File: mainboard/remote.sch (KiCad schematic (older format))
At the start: 14 parts, among them J1 Conn_01x03, J2 Conn_01x02, J4 Conn_01x03, J5 Conn_01x03, J6 Conn_01x02, J7 Conn_01x03, U7 COM-09032, U8 COM-09032

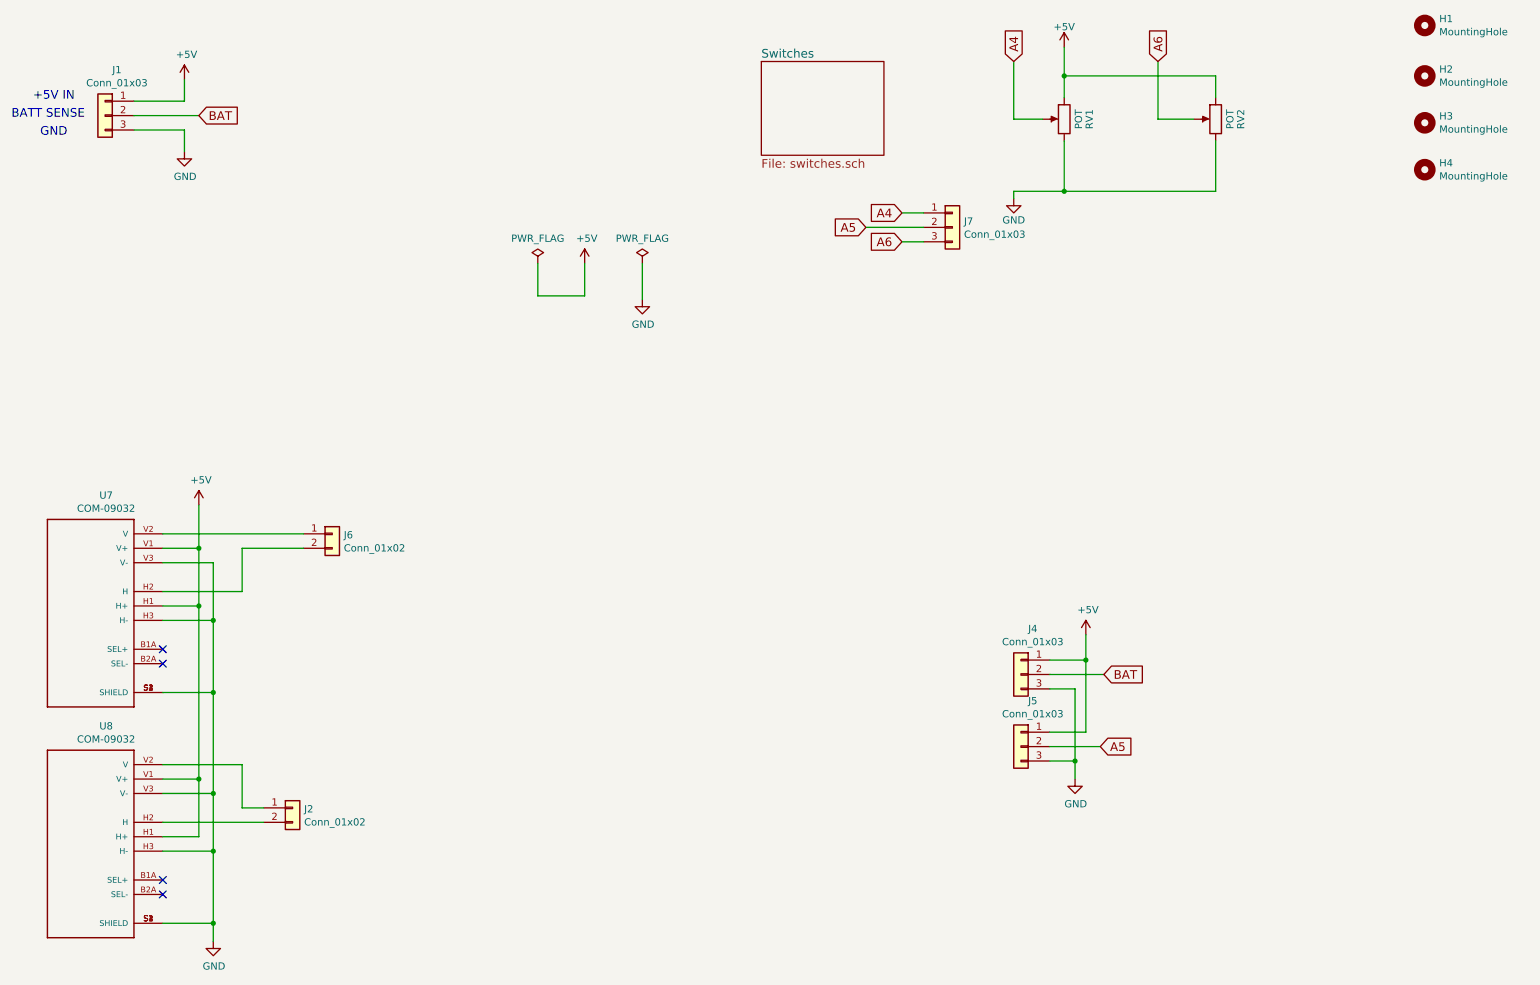
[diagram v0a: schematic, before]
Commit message: Update for I2C display.
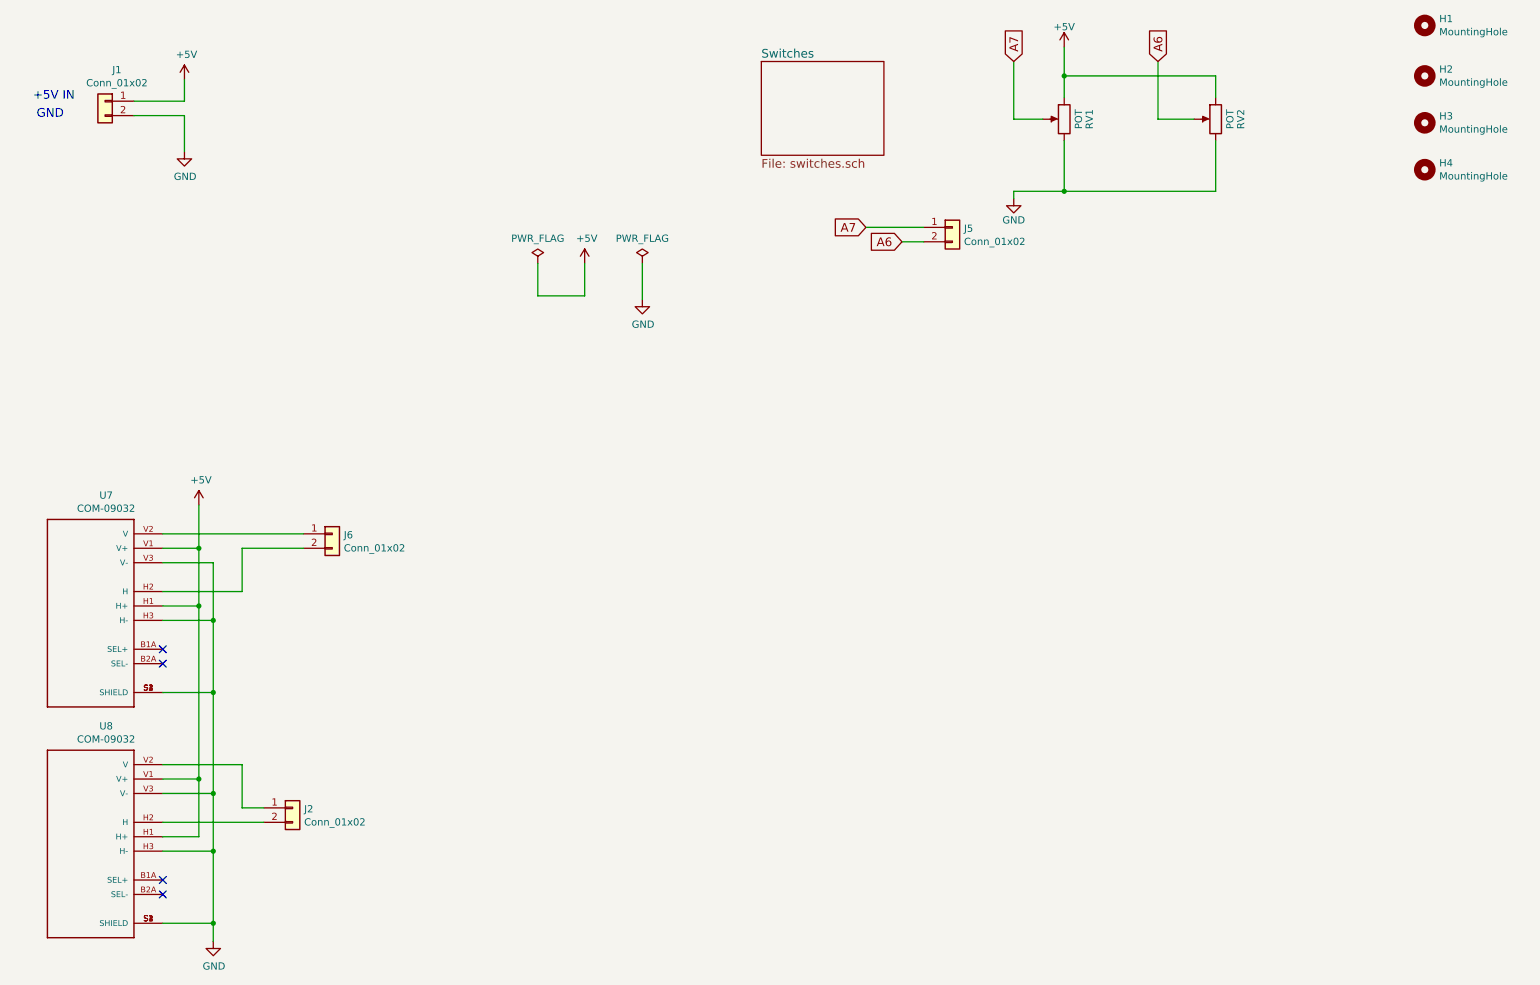
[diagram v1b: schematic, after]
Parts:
- removed J1, J4, J5, J7: Conn_01x03, Milling:JST_XH_B03B-XH-A_1x03_P2.50mm_Vertical_Milling, symbol Connector_Generic:Conn_01x03
- added J1, J5: Conn_01x02, Milling:JST_XH_B02B-XH-A_1x02_P2.50mm_Vertical_Milling, symbol Connector_Generic:Conn_01x02
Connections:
- net +5V: now also J1.1 (Pin_1)
- net A6: now also J5.2 (Pin_2)
- net GND: now also J1.2 (Pin_2)
- net A4 renamed A7
- net A7: now also J5.1 (Pin_1)
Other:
- note removed: "BATT SENSE"
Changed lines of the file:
@@
 	8700 1375 8450 1375
 Text GLabel 7450 975  1    60   Input ~ 0
-A4
+A7
 Text GLabel 8450 975  1    60   Input ~ 0
 A6
@@
 A6
 Text GLabel 6425 2125 0    60   Input ~ 0
-A5
-Text GLabel 6675 2025 0    60   Input ~ 0
-A4
+A7
 Wire Wire Line
 	7450 1875 7450 1925
@@
 	7800 1875 8850 1875
 $Comp
-L Connector_Generic:Conn_01x03 J1
-U 1 1 5E3721E4
-P 1150 1350
-F 0 "J1" H 1068 1667 50  0000 C CNN
-F 1 "Conn_01x03" H 1068 1576 50  0000 C CNN
-F 2 "Milling:JST_XH_B03B-XH-A_1x03_P2.50mm_Vertical_Milling" H 1150 1350 50  0001 C CNN
-F 3 "~" H 1150 1350 50  0001 C CNN
-	1    1150 1350
-	-1   0    0    -1
-$EndComp
-$Comp
 L power:+5V #PWR0109
 U 1 1 5E3728A7
@@
 	1    0    0    -1
 $EndComp
-Wire Wire Line
-	1700 1600 1700 1450
-Wire Wire Line
-	1700 1450 1350 1450
-Text GLabel 8050 5725 2    60   Input ~ 0
-A5
-Wire Wire Line
-	1800 1350 1350 1350
 Text Notes 650  1250 0    60   ~ 0
 +5V IN
-Text Notes 700  1500 0    60   ~ 0
+Text Notes 675  1375 0    60   ~ 0
 GND
-Text Notes 500  1375 0    60   ~ 0
-BATT SENSE
 $Comp
 L power:PWR_FLAG #FLG0101
@@
 	6825 2125 6425 2125
 Wire Wire Line
-	6675 2025 6825 2025
-Wire Wire Line
 	1550 4650 2100 4650
-$Comp
-L Connector_Generic:Conn_01x03 J4
-U 1 1 5E698090
-P 7500 5225
-F 0 "J4" H 7418 5542 50  0000 C CNN
-F 1 "Conn_01x03" H 7418 5451 50  0000 C CNN
-F 2 "Milling:JST_XH_B03B-XH-A_1x03_P2.50mm_Vertical_Milling" H 7500 5225 50  0001 C CNN
-F 3 "~" H 7500 5225 50  0001 C CNN
-	1    7500 5225
-	-1   0    0    -1
-$EndComp
-$Comp
-L Connector_Generic:Conn_01x03 J5
-U 1 1 5E698C2B
-P 7500 5725
-F 0 "J5" H 7418 6042 50  0000 C CNN
-F 1 "Conn_01x03" H 7418 5951 50  0000 C CNN
-F 2 "Milling:JST_XH_B03B-XH-A_1x03_P2.50mm_Vertical_Milling" H 7500 5725 50  0001 C CNN
-F 3 "~" H 7500 5725 50  0001 C CNN
-	1    7500 5725
-	-1   0    0    -1
-$EndComp
-$Comp
-L power:+5V #PWR0130
-U 1 1 5E6B17BB
-P 7950 4950
-F 0 "#PWR0130" H 7950 4800 50  0001 C CNN
-F 1 "+5V" H 7965 5123 50  0000 C CNN
-F 2 "" H 7950 4950 50  0001 C CNN
-F 3 "" H 7950 4950 50  0001 C CNN
-	1    7950 4950
-	1    0    0    -1
-$EndComp
-Wire Wire Line
-	7950 4950 7950 5125
-Wire Wire Line
-	7950 5625 7700 5625
-Wire Wire Line
-	7700 5125 7950 5125
-Connection ~ 7950 5125
-Wire Wire Line
-	7950 5125 7950 5625
-$Comp
-L power:GND #PWR0131
-U 1 1 5E6BD4D9
-P 7875 5950
-F 0 "#PWR0131" H 7875 5700 50  0001 C CNN
-F 1 "GND" H 7880 5777 50  0000 C CNN
-F 2 "" H 7875 5950 50  0001 C CNN
-F 3 "" H 7875 5950 50  0001 C CNN
-	1    7875 5950
-	1    0    0    -1
-$EndComp
-Wire Wire Line
-	7875 5950 7875 5825
-Wire Wire Line
-	7875 5325 7700 5325
-Wire Wire Line
-	7700 5825 7875 5825
-Connection ~ 7875 5825
-Wire Wire Line
-	7875 5825 7875 5325
-Wire Wire Line
-	8050 5725 7700 5725
-Text GLabel 8075 5225 2    60   Input ~ 0
-BAT
-Wire Wire Line
-	8075 5225 7700 5225
-Text GLabel 1800 1350 2    60   Input ~ 0
-BAT
 $Comp
 L Connector_Generic:Conn_01x02 J6
@@
 	2100 6150 2250 6150
 $Comp
-L Connector_Generic:Conn_01x03 J7
-U 1 1 5E7123B6
+L Connector_Generic:Conn_01x02 J1
+U 1 1 5E3EC8B6
+P 1150 1250
+F 0 "J1" H 1068 1467 50  0000 C CNN
+F 1 "Conn_01x02" H 1068 1376 50  0000 C CNN
+F 2 "Milling:JST_XH_B02B-XH-A_1x02_P2.50mm_Vertical_Milling" H 1150 1250 50  0001 C CNN
+F 3 "~" H 1150 1250 50  0001 C CNN
+	1    1150 1250
+	-1   0    0    -1
+$EndComp
+Wire Wire Line
+	1350 1350 1700 1350
+Wire Wire Line
+	1700 1350 1700 1600
+$Comp
+L Connector_Generic:Conn_01x02 J5
+U 1 1 5E3F203B
 P 7025 2125
-F 0 "J7" H 7105 2167 50  0000 L CNN
-F 1 "Conn_01x03" H 7105 2076 50  0000 L CNN
-F 2 "Milling:JST_XH_B03B-XH-A_1x03_P2.50mm_Vertical_Milling" H 7025 2125 50  0001 C CNN
+F 0 "J5" H 7105 2117 50  0000 L CNN
+F 1 "Conn_01x02" H 7105 2026 50  0000 L CNN
+F 2 "Milling:JST_XH_B02B-XH-A_1x02_P2.50mm_Vertical_Milling" H 7025 2125 50  0001 C CNN
 F 3 "~" H 7025 2125 50  0001 C CNN
 	1    7025 2125

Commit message: Fix joystick footprint.
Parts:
- U7, U8: footprint Remote:XDCR_COM-09032 -> Remote:AnalogJoystick_ALPS_10k
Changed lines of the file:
@@
 F 0 "U7" H 943 5517 50  0000 C CNN
 F 1 "COM-09032" H 943 5426 50  0000 C CNN
-F 2 "Remote:XDCR_COM-09032" H 1050 4750 50  0001 L BNN
+F 2 "Remote:AnalogJoystick_ALPS_10k" H 1050 4750 50  0001 L BNN
 F 3 "Manufacturer Recommendations" H 1050 4750 50  0001 L BNN
 F 4 "SparkFun Electronics" H 1050 4750 50  0001 L BNN "Field4"
@@
 F 0 "U8" H 943 7117 50  0000 C CNN
 F 1 "COM-09032" H 943 7026 50  0000 C CNN
-F 2 "Remote:XDCR_COM-09032" H 1050 6350 50  0001 L BNN
+F 2 "Remote:AnalogJoystick_ALPS_10k" H 1050 6350 50  0001 L BNN
 F 3 "Manufacturer Recommendations" H 1050 6350 50  0001 L BNN
 F 4 "SparkFun Electronics" H 1050 6350 50  0001 L BNN "Field4"
